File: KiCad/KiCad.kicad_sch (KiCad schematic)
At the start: 17 parts, among them M1 Right TT_Motor_DC, M2 Left TT_Motor_DC, U1 NUCLEO-F042K6, U2 KY_32I_IR_sensor, U3 KY_32I_IR_sensor, U4 Powerboost_1000_Basic, U6 ON/OFF switch, U7 L293D Dual Motor Driver

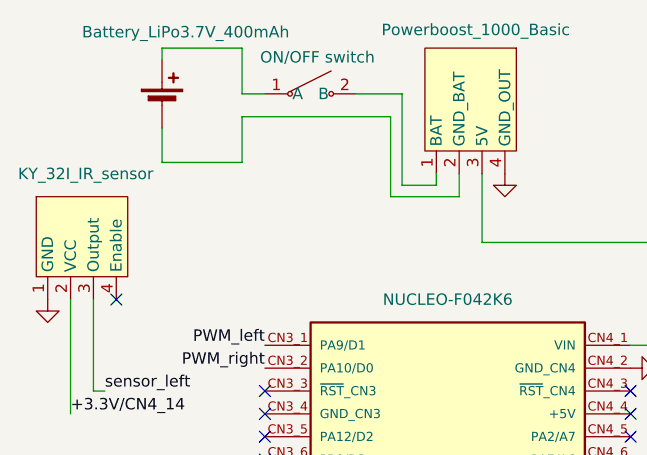
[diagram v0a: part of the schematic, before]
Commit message: Added images
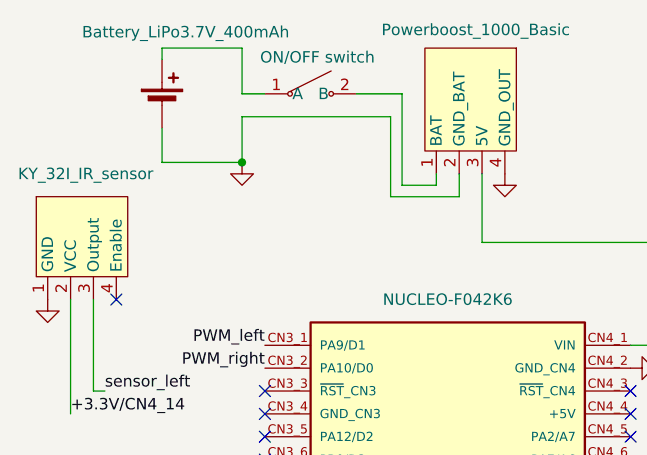
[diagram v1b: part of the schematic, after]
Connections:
- net GND: now also BT2.2 (-), U4.2 (GND_BAT)
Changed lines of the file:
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@@
+		(color 0 0 0 0)
+	)
+	(junction
+		(at 124.46 63.5)
+		(diameter 0)
 		(color 0 0 0 0)
 	)
@@
 					(unit 1)
 				)
+			)
+		)
+	)
+	(symbol
+		(lib_id "power:GND")
+		(at 124.46 63.5 0)
+		(unit 1)
+		(exclude_from_sim no)
+		(in_bom yes)
+		(on_board yes)
+		(dnp no)
+		(property "Reference" "#PWR017"
+			(at 124.46 69.85 0)
+			(effects
+				(font
+					(size 1.27 1.27)
+				)
+				(hide yes)
+			)
+		)
+		(property "Value" "GND"
+			(at 122.174 63.754 0)
+			(effects
+				(font
+					(size 1.27 1.27)
+				)
+				(hide yes)
+			)
+		)
+		(property "Footprint" ""
+			(at 124.46 63.5 0)
+			(effects
+				(font
+					(size 1.27 1.27)
+				)
+				(hide yes)
+			)
+		)
+		(property "Datasheet" ""
+			(at 124.46 63.5 0)
+			(effects
+				(font
+					(size 1.27 1.27)
+				)
+				(hide yes)
+			)
+		)
+		(property "Description" "Power symbol creates a global label with name \"GND\" , ground"
+			(at 124.46 63.5 0)
+			(effects
+				(font
+					(size 1.27 1.27)
+				)
+				(hide yes)
+			)
+		)
+		(pin "1"
+		)
+		(instances
+			(project "KiCad"
+				(path "/bd8a75cf-984f-4cb2-9f9a-71d40c52f87c"
+					(reference "#PWR017")
+					(unit 1)
+				)
